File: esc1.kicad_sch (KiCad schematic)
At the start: 68 parts, among them J3 Pad Terminals, J4 Signal, Q1 NMOS, Q2 NMOS, Q3 NMOS, Q4 NMOS, Q5 NMOS, Q6 NMOS, U10 INA180A3, U11 IRS21867S, U12 INA180A3, U13 STM32F303CBTx, U7 IRS21867S, U8 INA180A3, U9 IRS21867S

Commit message: ESC Schematic Update
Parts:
- removed C15, C20: 10uF, symbol Device:C_Polarized
- added BOOT0_SW: BOOT_Push, symbol Switch:SW_Push
- added C15, C20, C40: 100n, symbol Device:C
- added C41, C42: 1u, symbol Device:C_Polarized
- added D14, D15: LED, symbol Device:LED
- added R30: 10k, symbol Device:R
- added R31: 20k, symbol Device:R
- added R32, R33: 150, symbol Device:R
- added ST-Link: ST-Conn, symbol Connector_Generic:Conn_02x04_Odd_Even
- C16, C21, C26: value 2.2uF -> 2.2u
- C17, C23, C28: value 100nF -> 100n
- C25: value 10uF -> 1u
- R14, R19, R26: value 6m -> 0.6m
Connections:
- net +ESC: now also C15.1, C20.1, C40.1, C41.1, C42.1
- net -ESC: now also C15.2, C20.2, C40.2, C41.2, C42.2
- net SWCLK: now also ST-Link.4 (Pin_4)
- net SWDIO: now also ST-Link.8 (Pin_8)
- net NRST: now reaches C39.2, NRST_SW.1, U13.7 (NRST)
- net NRST: now also ST-Link.7 (Pin_7)
- net at U13.10 (PA0): now also R32.1
- net at U13.11 (PA1): now also R33.1
- net at U13.44 (BOOT0): now also R30.2
- net +3V3ESC renamed +3V3MCU
- net +3V3MCU: now also BOOT0_SW.1, ST-Link.1 (Pin_1), ST-Link.2 (Pin_2)
- net -3V3ESC renamed -3V3MCU
- net -3V3MCU: now also D14.1 (K), D15.1 (K), R31.1, ST-Link.5 (Pin_5), ST-Link.6 (Pin_6)
- net NJTRST: no longer names the net of U13.40 (PB4)
- new net: BOOT0_SW.2, R30.1, R31.2
- new net: D14.2 (A), R32.2
- new net: D15.2 (A), R33.2
- no-connect marks 1 -> 2
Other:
- note added: "Phase A"
- note added: "Phase B"
- note added: "Phase C"
- note added: "STM32F303CBTx"
- note added: "TIM1_CH1"
- note added: "TIM1_CH1N"
- note added: "TIM1_CH2"
- note added: "TIM1_CH2N"
- note added: "TIM1_CH3"
- note added: "TIM1_CH3N"
- moved on the sheet: C16, C17, C18, C19, C21, C22, C23, C24, C25, C26, C27, C28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

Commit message: ESC Update with Specifications
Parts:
- removed C22: 10n, symbol Device:C
- removed C25, C41: 1u, symbol Device:C_Polarized
- removed C26: 2.2u, symbol Device:C_Polarized
- removed C29: 1n, symbol Device:C
- removed C40: 100n, symbol Device:C
- removed D10, D12, D8: 1N4148WT, Diode_SMD:D_SOD-523, symbol Diode:1N4148WT
- removed U10, U12: INA180A3, Package_TO_SOT_SMD:SOT-23-5, symbol Amplifier_Current:INA180A3
- removed U11, U9: IRS21867S, Package_SO:SOIC-8_3.9x4.9mm_P1.27mm, symbol Driver_FET:IRS21867S
- added 12V_SD1: XL1509-12, Package_SO:SOIC-8_3.9x4.9mm_P1.27mm, symbol Regulator_Switching:XL1509-12
- added C22, C40: 2.2u, symbol Device:C_Polarized
- added C25, C49: 10n, symbol Device:C
- added C26, C47, C48, C50: 100n, symbol Device:C
- added C29: 1u, symbol Device:C_Polarized
- added C41, C44, C46: 1u, symbol Device:C
- added C43: 470u, symbol Device:C_US
- added C45: 180u, symbol Device:C_US
- added C51: 1n, symbol Device:C
- added D10, D12, D8: 1N5819WS, Diode_SMD:D_SOD-323, symbol Diode:1N5819WS
- added D16: 1N5820, Diode_THT:D_DO-201AD_P15.24mm_Horizontal, symbol Diode:1N5820
- added D17: BuckLED, symbol Device:LED
- added L5: 68u, symbol Device:L
- added R34: 220, symbol Device:R
- added R35: 1k, symbol Device:R
- added TVS1: SMF30A, Diode_SMD:D_SMF, symbol Diode:SMF30A
- added U1, U6: IRS21867S, Package_SO:SOIC-8_3.9x4.9mm_P1.27mm, symbol Driver_FET:IRS21867S
- added U4, U9: INA180A3, Package_TO_SOT_SMD:SOT-23-5, symbol Amplifier_Current:INA180A3
- C21: value 2.2u -> 1u
- C23: value 100n -> 1u
- C24: value 1n -> 100n
- C27: value 10n -> 1n
- C30: value C_ESC -> 1000u
- C33, C34, C35, C37, C39: value 0.1u -> 100n
- R14, R19, R26: value 0.6m -> 6E-4
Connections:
- net +3V3MCU: now also C17.1, U8.5 (V+), C26.1, C50.1, U4.5 (V+), U9.5 (V+)
- net +ESC: now also 12V_SD1.1 (VIN), C43.1, C44.1, TVS1.1 (A1); no longer C15.1, C20.1, C42.1, U7.1 (VCC)
- net -ESC: now also C21.2, 12V_SD1.4 (~{EN}), 12V_SD1.5 (GND), 12V_SD1.6 (GND), 12V_SD1.7 (GND), 12V_SD1.8 (GND), C25.1, C26.2, C29.2, C43.2, C44.2, C45.2, C49.1, C50.2, D16.2 (A), R35.2, TVS1.2 (A2), U1.4 (COM), U4.4 (-), U6.4 (COM), U9.4 (-); no longer C23.2, C27.1
- net A_Phase: now also C46.2, C47.2
- net B_Phase: now also C23.2, C24.2, C22.2, U1.6 (VS); no longer C21.2
- net C_Phase: now also C40.2, C41.2, C48.2, U6.6 (VS)
- net MCU_BFB: now also C25.2
- net MCU_BH: now also U1.2 (HIN)
- net MCU_BI: now also C27.1; no longer C24.1
- net MCU_BL: now also U1.3 (LIN)
- net MCU_CFB: now also C49.2; no longer C27.2
- net MCU_CH: now also U6.2 (HIN)
- net MCU_CI: now also C51.1
- net MCU_CL: now also U6.3 (LIN)
- net SIG_ESC: now also R34.2
- net at R17.1: now also U1.5 (LO)
- net at Q4.3 (S), R18.2, R19.1: now also U4.3 (+)
- net at R24.1: now also U6.5 (LO)
- net at R23.1: now also U6.7 (HO)
- net at R29.1: now also U9.1
- net at Q6.3 (S), R25.2, R26.1: now also U9.3 (+)
- net +12V: now reaches C21.1
- net +12V: now also C15.1, C20.1, C28.1, C42.1, U7.1 (VCC), 12V_SD1.3 (FB), C29.1, C45.1, D10.2 (A), D12.2 (A), D17.2 (A), D8.2 (A), L5.2, U1.1 (VCC), U6.1 (VCC)
- net at R22.1: now also U4.1
- net at R16.1: now also U1.7 (HO)
- net at U13.13 (PA3): now also R34.1
- net at C16.1, U7.8 (VB): now also C46.1, C47.1, D8.1 (K)
- removed net +3V3: C17.1, C23.1, C28.1, U8.5 (V+)
- new net: C40.1, C41.1, C48.1, D12.1 (K), U6.8 (VB)
- new net: C22.1, C23.1, C24.1, D10.1 (K), U1.8 (VB)
- new net: D17.1 (K), R35.1
- new net: 12V_SD1.2 (OUT), D16.1 (K), L5.1
- new net: C27.2, U4.2 (GND)
- new net: C51.2, U9.2 (GND)
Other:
- note added: "12V Driver Buck"
- note added: "ADC1_CH4"
- note added: "Buck Converter"
- note added: "Connectors"
- note added: "Dissipation Characteristics: 50A (MAX): 5.25W (246.75°C) 30A: 1.89W (88.83°C) 20A: 0.84W (39.48°C) 10A: 0.21W (9.87°C)"
- note added: "Each Gate Driver: ~5mA Quiescent: 10mA Total Load: 40mA (0.48W) Efficiency: 90% (Vin=25V, Vout=12V, Iout=2A) Input Draw: 22.22mA (0.53W) Dissipation: 0.05W (5°C)"
- note added: "Gate Drivers"
- note added: "LEDs 5mA x 2"
- note added: "MOSFETs"
- note added: "Max Drain Current: 1.2A Switching Time: 49.58nS Maximum Frequency: 20MHz"
- note added: "Max Drain Output: 4A Switching Time: 170nS Maximum Frequency: 5.88MHz"
- note added: "Power Input & Protection"
- moved on the sheet: C30, J3, J4, Q1, Q2, R11, R14, R9

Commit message: ESC Final Draft 1
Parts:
- added R36, R37, R38: 100, symbol Device:R
- R12, R21, R28: value 30k -> 7k
- R13, R20, R27: value 4k -> 1k
- R32, R33: value 150 -> 220
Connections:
- net MCU_AFB: now also U13.14 (PA4), R36.2; no longer C19.2, D9.2, R12.1, R13.2
- net MCU_AI: now also U13.25 (PB12)
- net MCU_BFB: now also U13.15 (PA5), R37.2; no longer C25.2, D11.2, R20.2, R21.1
- net MCU_BI: now also U13.26 (PB13)
- net MCU_CFB: now also U13.16 (PA6), R38.2; no longer C49.2, D13.2, R27.2, R28.1
- net MCU_CI: now also U13.27 (PB14)
- new net: C25.2, D11.2, R20.2, R21.1, R37.1
- new net: C49.2, D13.2, R27.2, R28.1, R38.1
- new net: C19.2, D9.2, R12.1, R13.2, R36.1
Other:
- note added: "ADC2_CH1"
- note added: "ADC2_CH2"
- note added: "ADC2_CH3"
- note added: "ADC4_CH3"
- note added: "ADC4_CH4"
- note added: "ADC4_CH5"

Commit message: ESC Update
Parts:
- removed C16, C22, C40: 2.2u, symbol Device:C_Polarized
- removed C23, C46: 1u, symbol Device:C
- removed C24, C47, C48: 100n, symbol Device:C
- added C16, C22: 1u, symbol Device:C
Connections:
- net A_Phase: now also C16.2
- net B_Phase: now also C22.2
- net at D10.1 (K), U1.8 (VB): now also C22.1
- net at D8.1 (K), U7.8 (VB): now also C16.1
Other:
- note added: "Max Voltage Drop: 0.03V Dissipation: 1.5W (7.13°)"
- note added: "Shunts"
- moved on the sheet: C41

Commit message: ESC Update & Finalization Draft
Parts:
- removed C21, C42: 1u, symbol Device:C_Polarized
- removed C43: 470u, symbol Device:C_US
- removed C45: 180u, symbol Device:C_US
- removed D11, D13, D9: SMBJ33A, PCM_JLCPCB:D_SMB, symbol PCM_JLCPCB-Diodes:TVS-Uni,SMBJ33A
- added C21, C23, C24: 1u, symbol Device:C
- added C40: 180u, symbol Device:C_Polarized
- C18, C27, C51: value 1n -> 22n
- C19, C25, C49: value 10n -> 22n
- C29: value 1u -> 470u
- D14, D15: footprint (none) -> LED_SMD:LED_0805_2012Metric
- D16: value 1N5820 -> SS34
- NMOS1: renamed from Q1; value NMOS -> HYG025N06LS1C2
- NMOS2: renamed from Q2; value NMOS -> HYG025N06LS1C2
- NMOS3: renamed from Q3; value NMOS -> HYG025N06LS1C2
- NMOS4: renamed from Q4; value NMOS -> HYG025N06LS1C2
- NMOS5: renamed from Q5; value NMOS -> HYG025N06LS1C2
- NMOS6: renamed from Q6; value NMOS -> HYG025N06LS1C2
- R11, R18, R25: value 18k -> 47k
- R15, R22, R29: value 1k -> 220
- R16: footprint (none) -> Resistor_SMD:R_0805_2012Metric
- R36, R37, R38: value 100 -> 220
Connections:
- net +12V: now also C21.1, C23.1, C24.1, C40.1; no longer C29.1
- net +ESC: now also C29.1
- net -ESC: now also C21.2, C23.2, C24.2, C40.2
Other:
- note added: "Drain Output (MAX): 4A Switching Time: 170nS Maximum Frequency: 5.88MHz"
- note added: "LEDs 15mA x 2"
- note added: "Voltage Drop (MAX): 0.03V Dissipation: 1.5W (7.13°)"
- note removed: "LEDs 5mA x 2"
- note removed: "Max Drain Output: 4A Switching Time: 170nS Maximum Frequency: 5.88MHz"
- note removed: "Max Voltage Drop: 0.03V Dissipation: 1.5W (7.13°)"

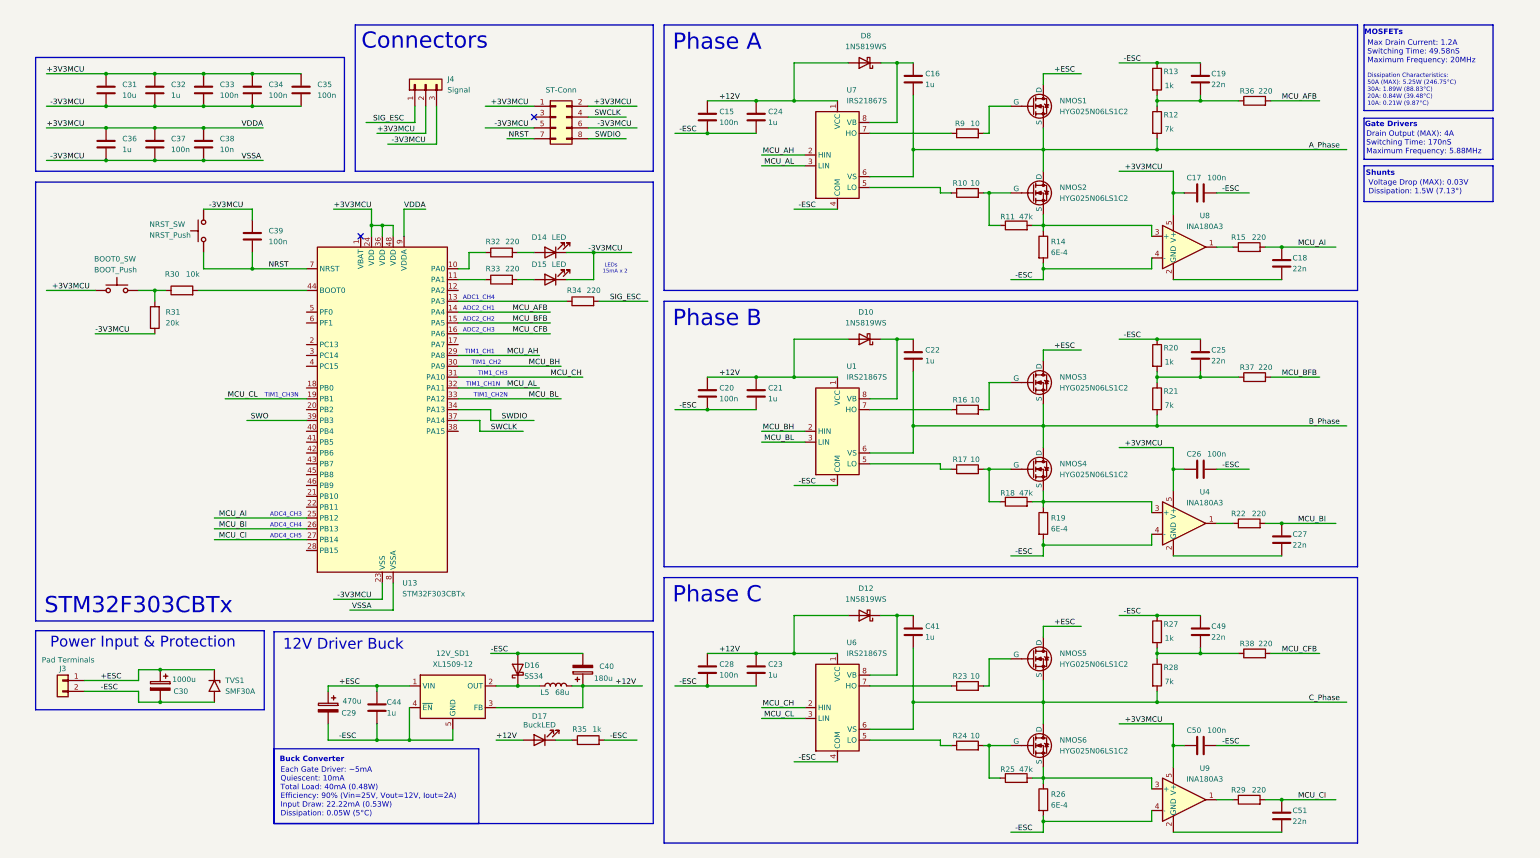
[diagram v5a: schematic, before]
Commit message: Less bulky switching regulator for the ESC drivers, PCB update.
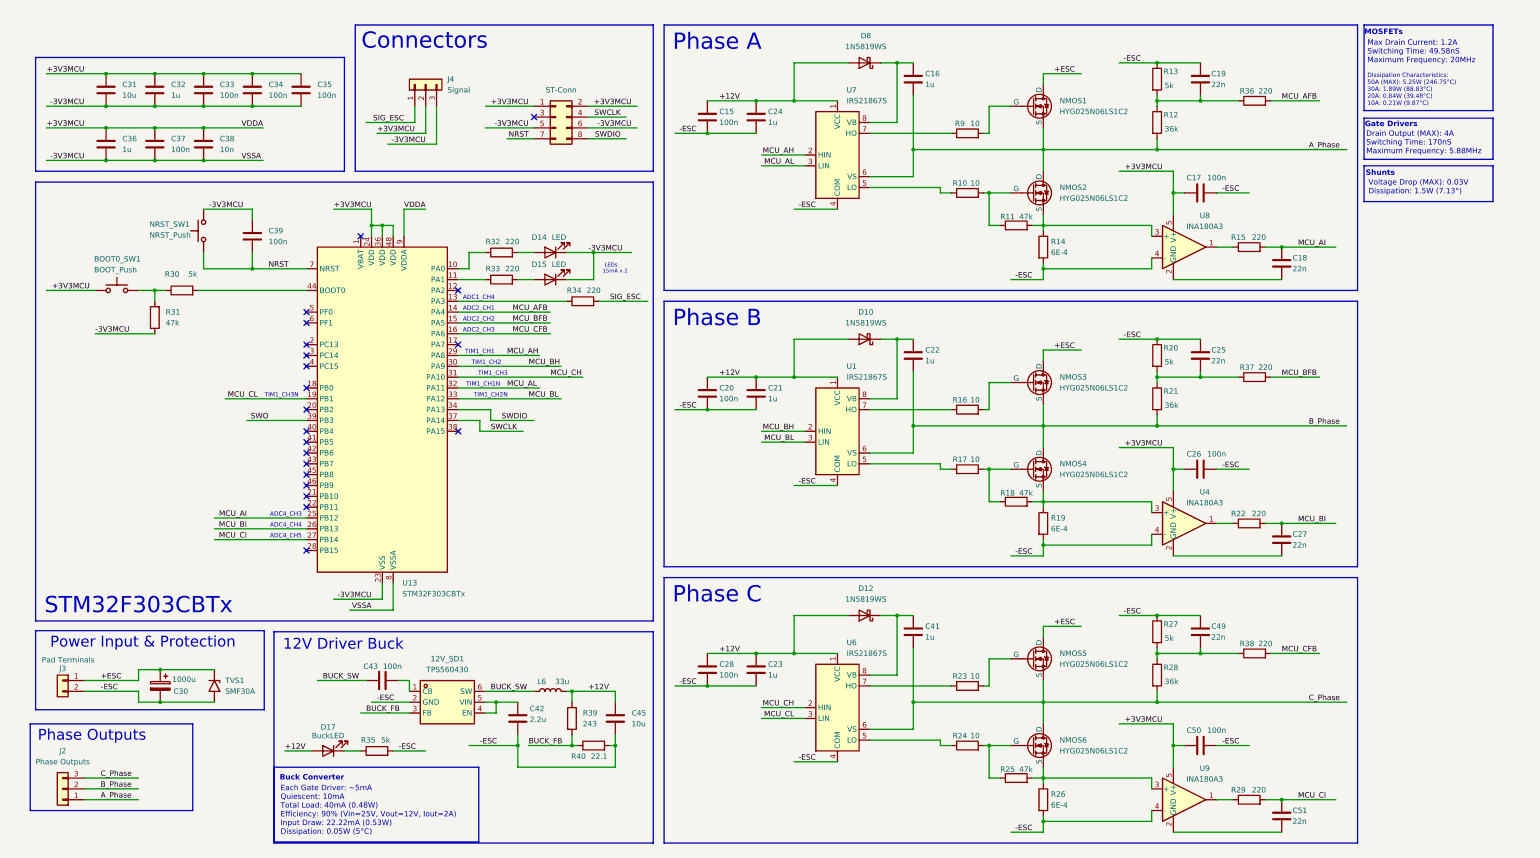
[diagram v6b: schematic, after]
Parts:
- removed 12V_SD1: XL1509-12, Package_SO:SOIC-8_3.9x4.9mm_P1.27mm, symbol Regulator_Switching:XL1509-12
- removed C29: 470u, symbol Device:C_Polarized
- removed C40: 180u, symbol Device:C_Polarized
- removed C44: 1u, symbol Device:C
- removed D16: SS34, Diode_THT:D_DO-201AD_P15.24mm_Horizontal, symbol Diode:1N5820
- removed L5: 68u, symbol Device:L
- added 12V_SD1: TPS560430, easyeda2kicad:SOT-23-6_L2.9-W1.6-P0.95-LS2.8-BL, symbol easyeda2kicad:TPS560430XDBVR
- added C42: 2.2u, Capacitor_SMD:C_0805_2012Metric, symbol Device:C
- added C43: 100n, Capacitor_SMD:C_0805_2012Metric, symbol Device:C
- added C45: 10u, Capacitor_SMD:C_0805_2012Metric, symbol Device:C
- added J2: Phase Outputs, CustomFPs:ESC Outputs, symbol Connector_Generic:Conn_01x03
- added L6: 33u, easyeda2kicad:IND-SMD_L3.0-W3.0_LQH3NPN2R2NG0L, symbol Device:L
- added R39: 243, easyeda2kicad:R0805, symbol Device:R
- added R40: 22.1, easyeda2kicad:R0805, symbol Device:R
- BOOT0_SW1: renamed from BOOT0_SW; footprint (none) -> easyeda2kicad:SW-SMD_4P-L3.5-W3.0-P1.50-LS4.7
- C15, C17, C20, C26, C28, C33, C34, C35, C37, C39, C50: footprint (none) -> easyeda2kicad:C0805
- C16, C18, C19, C21, C22, C23, C24, C25, C27, C31, C32, C36, C38, C41, C49, C51: footprint (none) -> Capacitor_SMD:C_0805_2012Metric
- C30: footprint (none) -> easyeda2kicad:CAP-TH_BD12.5-P5.00-D0.6-FD
- D10, D12, D8: footprint Diode_SMD:D_SOD-323 -> easyeda2kicad:SOD-323_L1.8-W1.3-LS2.5-RD
- D17: footprint (none) -> LED_SMD:LED_0805_2012Metric
- J3: footprint Library:VCC Pads -> CustomFPs:Battery Inputs
- J4: footprint (none) -> Connector_PinHeader_2.54mm:PinHeader_1x03_P2.54mm_Horizontal
- NMOS1, NMOS2, NMOS3, NMOS4, NMOS5, NMOS6: footprint (none) -> easyeda2kicad:DFN-8_L5.9-W5.2-P1.27-LS6.2-BL
- NRST_SW1: renamed from NRST_SW; footprint (none) -> easyeda2kicad:SW-SMD_4P-L3.5-W3.0-P1.50-LS4.7
- R10, R11, R15, R17, R18, R22, R23, R24, R25, R29, R32, R33, R34, R36, R37, R38, R9: footprint (none) -> easyeda2kicad:R0805
- R12, R21, R28: value 7k -> 36k; footprint (none) -> easyeda2kicad:R0805
- R13, R20, R27, R35: value 1k -> 5k; footprint (none) -> easyeda2kicad:R0805
- R14, R19, R26: footprint (none) -> easyeda2kicad:RES-SMD_L6.4-W3.2_LRS2512
- R16: footprint Resistor_SMD:R_0805_2012Metric -> easyeda2kicad:R0805
- R30: value 10k -> 5k; footprint (none) -> easyeda2kicad:R0805
- R31: value 20k -> 47k; footprint (none) -> easyeda2kicad:R0805
- ST-Link1: renamed from ST-Link; footprint (none) -> Connector_PinHeader_2.54mm:PinHeader_2x04_P2.54mm_Vertical
- TVS1: footprint Diode_SMD:D_SMF -> easyeda2kicad:SOD-123FL_L2.7-W1.8-LS3.8-RD
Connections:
- net +12V: now also C45.1, L6.2, R39.1
- net -ESC: now also 12V_SD1.2 (GND), C42.2, C45.2, R40.2
- net A_Phase: now also J2.1 (Pin_1)
- net B_Phase: now also J2.2 (Pin_2)
- net C_Phase: now also J2.3 (Pin_3)
- new net: 12V_SD1.1 (CB), C43.2
- new net: 12V_SD1.4 (EN), 12V_SD1.5 (VIN), C42.1
- new net BUCK_FB: 12V_SD1.3 (FB), R39.2, R40.1
- new net BUCK_SW: 12V_SD1.6 (SW), C43.1, L6.1
- no-connect marks 2 -> 21
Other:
- note added: "Phase Outputs"
- moved on the sheet: D17, R35
